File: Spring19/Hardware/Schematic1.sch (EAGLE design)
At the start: 18 parts

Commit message: Attempt 1 at routing
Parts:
- added R5: 1k, SparkFun-Resistors:1KOHM-0603-1/10W-1%
- added RELAYLEFT, RELAYRIGHT: (no value), con-lstb:MA07-1
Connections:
- new net N$14: IC1.2, R5.2, RELAYLEFT.1
- net GND: now also R5.1, RELAYLEFT.7
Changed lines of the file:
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@@
 <part name="GND3" library="supply1" library_urn="urn:adsk.eagle:library:371" deviceset="GND" device=""/>
 <part name="P+3" library="supply1" library_urn="urn:adsk.eagle:library:371" deviceset="VCC" device=""/>
+<part name="RELAYRIGHT" library="con-lstb" library_urn="urn:adsk.eagle:library:162" deviceset="MA07-1" device="" package3d_urn="urn:adsk.eagle:package:8341/1"/>
+<part name="RELAYLEFT" library="con-lstb" library_urn="urn:adsk.eagle:library:162" deviceset="MA07-1" device="" package3d_urn="urn:adsk.eagle:package:8341/1"/>
+<part name="GND9" library="supply1" library_urn="urn:adsk.eagle:library:371" deviceset="GND" device=""/>
+<part name="R5" library="SparkFun-Resistors" library_urn="urn:adsk.eagle:library:532" deviceset="1KOHM" device="-0603-1/10W-1%" package3d_urn="urn:adsk.eagle:package:39650/1" value="1k"/>
+<part name="GND10" library="supply1" library_urn="urn:adsk.eagle:library:371" deviceset="GND" device=""/>
 </parts>
 <sheets>
@@
 <instance part="P+3" gate="VCC" x="106.68" y="38.1" smashed="yes" rot="MR0">
 <attribute name="VALUE" x="109.22" y="35.56" size="1.778" layer="96" rot="MR90"/>
+</instance>
+<instance part="RELAYRIGHT" gate="1" x="187.96" y="-66.04" smashed="yes">
+<attribute name="VALUE" x="186.69" y="-78.74" size="1.778" layer="96"/>
+<attribute name="NAME" x="186.69" y="-55.118" size="1.778" layer="95"/>
+</instance>
+<instance part="RELAYLEFT" gate="1" x="182.88" y="-66.04" smashed="yes" rot="R180">
+<attribute name="VALUE" x="184.15" y="-53.34" size="1.778" layer="96" rot="R180"/>
+<attribute name="NAME" x="184.15" y="-76.962" size="1.778" layer="95" rot="R180"/>
+</instance>
+<instance part="GND9" gate="1" x="167.64" y="-73.66" smashed="yes" rot="MR90">
+<attribute name="VALUE" x="165.1" y="-76.2" size="1.778" layer="96" rot="MR90"/>
+</instance>
+<instance part="R5" gate="G$1" x="157.48" y="-58.42" smashed="yes" rot="MR90">
+<attribute name="NAME" x="159.004" y="-58.42" size="1.778" layer="95" font="vector" rot="MR90" align="bottom-center"/>
+<attribute name="VALUE" x="155.956" y="-58.42" size="1.778" layer="96" font="vector" rot="MR90" align="top-center"/>
+</instance>
+<instance part="GND10" gate="1" x="157.48" y="-68.58" smashed="yes" rot="MR0">
+<attribute name="VALUE" x="160.02" y="-71.12" size="1.778" layer="96" rot="MR0"/>
 </instance>
 </instances>
@@
 <pinref part="GND3" gate="1" pin="GND"/>
 <pinref part="IC1" gate="G$1" pin="GND@3"/>
+</segment>
+<segment>
+<pinref part="GND9" gate="1" pin="GND"/>
+<wire x1="175.26" y1="-73.66" x2="170.18" y2="-73.66" width="0.1524" layer="91"/>
+<pinref part="RELAYLEFT" gate="1" pin="7"/>
+</segment>
+<segment>
+<pinref part="GND10" gate="1" pin="GND"/>
+<wire x1="157.48" y1="-63.5" x2="157.48" y2="-66.04" width="0.1524" layer="91"/>
+<pinref part="R5" gate="G$1" pin="1"/>
 </segment>
 </net>
@@
 </segment>
 </net>
+<net name="N$14" class="0">
+<segment>
+<pinref part="RELAYLEFT" gate="1" pin="1"/>
+<wire x1="175.26" y1="-58.42" x2="175.26" y2="-53.34" width="0.1524" layer="91"/>
+<wire x1="175.26" y1="-53.34" x2="157.48" y2="-53.34" width="0.1524" layer="91"/>
+<wire x1="157.48" y1="-53.34" x2="134.62" y2="-53.34" width="0.1524" layer="91"/>
+<wire x1="134.62" y1="-53.34" x2="134.62" y2="17.78" width="0.1524" layer="91"/>
+<pinref part="IC1" gate="G$1" pin="2"/>
+<wire x1="134.62" y1="17.78" x2="129.54" y2="17.78" width="0.1524" layer="91"/>
+<pinref part="R5" gate="G$1" pin="2"/>
+<junction x="157.48" y="-53.34"/>
+</segment>
+</net>

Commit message: Finish routing
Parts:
- removed C1, C2: 22pF, SparkFun-Capacitors:22PF-0603-50V-5%
- removed CLOCK: 16MHz, SparkFun-Clocks:CRYSTAL-16MHZPTH-HC49US
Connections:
- removed net N$11: C2.2, CLOCK.1
- removed net N$13: C1.2, CLOCK.2
- net GND: no longer C1.1, C2.1
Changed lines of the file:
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@@
 <part name="SWITCH3" library="pinhead" library_urn="urn:adsk.eagle:library:325" deviceset="PINHD-1X2" device="" package3d_urn="urn:adsk.eagle:package:22435/2"/>
 <part name="CAP1188" library="pinhead" library_urn="urn:adsk.eagle:library:325" deviceset="PINHD-2X13" device="" package3d_urn="urn:adsk.eagle:package:22418/2"/>
-<part name="CLOCK" library="SparkFun-Clocks" library_urn="urn:adsk.eagle:library:511" deviceset="CRYSTAL-16MHZ" device="PTH-HC49US" package3d_urn="urn:adsk.eagle:package:37515/1" value="16MHz"/>
-<part name="C1" library="SparkFun-Capacitors" library_urn="urn:adsk.eagle:library:510" deviceset="22PF" device="-0603-50V-5%" package3d_urn="urn:adsk.eagle:package:37414/1" value="22pF"/>
-<part name="C2" library="SparkFun-Capacitors" library_urn="urn:adsk.eagle:library:510" deviceset="22PF" device="-0603-50V-5%" package3d_urn="urn:adsk.eagle:package:37414/1" value="22pF"/>
-<part name="GND6" library="supply1" library_urn="urn:adsk.eagle:library:371" deviceset="GND" device=""/>
 <part name="P+1" library="supply1" library_urn="urn:adsk.eagle:library:371" deviceset="VCC" device=""/>
 <part name="GND2" library="supply1" library_urn="urn:adsk.eagle:library:371" deviceset="GND" device=""/>
@@
 <attribute name="VALUE" x="196.85" y="-2.54" size="1.778" layer="96"/>
 </instance>
-<instance part="CLOCK" gate="G$1" x="139.7" y="-66.04" smashed="yes" rot="R90">
-<attribute name="NAME" x="137.668" y="-66.04" size="1.778" layer="95" font="vector" rot="R90" align="bottom-center"/>
-<attribute name="VALUE" x="141.732" y="-66.04" size="1.778" layer="96" font="vector" rot="R90" align="top-center"/>
-</instance>
-<instance part="C1" gate="G$1" x="132.08" y="-63.5" smashed="yes" rot="R90">
-<attribute name="NAME" x="129.159" y="-61.976" size="1.778" layer="95" font="vector" rot="R90"/>
-<attribute name="VALUE" x="134.239" y="-61.976" size="1.778" layer="96" font="vector" rot="R90"/>
-</instance>
-<instance part="C2" gate="G$1" x="132.08" y="-68.58" smashed="yes" rot="R90">
-<attribute name="NAME" x="129.159" y="-67.056" size="1.778" layer="95" font="vector" rot="R90"/>
-<attribute name="VALUE" x="134.239" y="-67.056" size="1.778" layer="96" font="vector" rot="R90"/>
-</instance>
-<instance part="GND6" gate="1" x="121.92" y="-68.58" smashed="yes">
-<attribute name="VALUE" x="119.38" y="-71.12" size="1.778" layer="96"/>
-</instance>
 <instance part="P+1" gate="VCC" x="218.44" y="-7.62" smashed="yes" rot="MR0">
 <attribute name="VALUE" x="220.98" y="-10.16" size="1.778" layer="96" rot="MR90"/>
@@
 </net>
 <net name="GND" class="0">
-<segment>
-<pinref part="C1" gate="G$1" pin="1"/>
-<pinref part="C2" gate="G$1" pin="1"/>
-<wire x1="127" y1="-63.5" x2="127" y2="-66.04" width="0.1524" layer="91"/>
-<wire x1="127" y1="-66.04" x2="127" y2="-68.58" width="0.1524" layer="91"/>
-<wire x1="127" y1="-66.04" x2="121.92" y2="-66.04" width="0.1524" layer="91"/>
-<junction x="127" y="-66.04"/>
-<pinref part="GND6" gate="1" pin="GND"/>
-</segment>
 <segment>
 <pinref part="R1" gate="G$1" pin="2"/>
@@
 </segment>
 </net>
-<net name="N$11" class="0">
-<segment>
-<wire x1="134.62" y1="-68.58" x2="139.7" y2="-68.58" width="0.1524" layer="91"/>
-<pinref part="CLOCK" gate="G$1" pin="1"/>
-<pinref part="C2" gate="G$1" pin="2"/>
-</segment>
-</net>
-<net name="N$13" class="0">
-<segment>
-<pinref part="CLOCK" gate="G$1" pin="2"/>
-<pinref part="C1" gate="G$1" pin="2"/>
-<wire x1="139.7" y1="-63.5" x2="134.62" y2="-63.5" width="0.1524" layer="91"/>
-</segment>
-</net>

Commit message: Add through holes for plug
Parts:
- added X1: SSW-101-02-G-D, con-samtec:SSW-101-02-G-D
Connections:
- new net N$11: RELAYRIGHT.6, X1-1.1
- new net N$13: RELAYRIGHT.2, X1-2.1
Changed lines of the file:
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@@
 <part name="R5" library="SparkFun-Resistors" library_urn="urn:adsk.eagle:library:532" deviceset="1KOHM" device="-0603-1/10W-1%" package3d_urn="urn:adsk.eagle:package:39650/1" value="1k"/>
 <part name="GND10" library="supply1" library_urn="urn:adsk.eagle:library:371" deviceset="GND" device=""/>
+<part name="X1" library="con-samtec" library_urn="urn:adsk.eagle:library:184" deviceset="SSW-101-02-G" device="-D"/>
 </parts>
 <sheets>
@@
 <instance part="GND10" gate="1" x="157.48" y="-68.58" smashed="yes" rot="MR0">
 <attribute name="VALUE" x="160.02" y="-71.12" size="1.778" layer="96" rot="MR0"/>
+</instance>
+<instance part="X1" gate="-1" x="215.9" y="-58.42" smashed="yes">
+<attribute name="VALUE" x="213.36" y="-55.88" size="1.778" layer="96"/>
+<attribute name="NAME" x="212.852" y="-57.658" size="1.524" layer="95" rot="R180"/>
+</instance>
+<instance part="X1" gate="-2" x="236.22" y="-58.42" smashed="yes">
+<attribute name="NAME" x="233.172" y="-57.658" size="1.524" layer="95" rot="R180"/>
 </instance>
 </instances>
@@
 </segment>
 </net>
+<net name="N$11" class="0">
+<segment>
+<pinref part="RELAYRIGHT" gate="1" pin="6"/>
+<wire x1="195.58" y1="-60.96" x2="218.44" y2="-60.96" width="0.1524" layer="91"/>
+<pinref part="X1" gate="-1" pin="1"/>
+<wire x1="218.44" y1="-60.96" x2="218.44" y2="-58.42" width="0.1524" layer="91"/>
+</segment>
+</net>
+<net name="N$13" class="0">
+<segment>
+<pinref part="X1" gate="-2" pin="1"/>
+<wire x1="238.76" y1="-58.42" x2="238.76" y2="-71.12" width="0.1524" layer="91"/>
+<pinref part="RELAYRIGHT" gate="1" pin="2"/>
+<wire x1="238.76" y1="-71.12" x2="195.58" y2="-71.12" width="0.1524" layer="91"/>
+</segment>
+</net>

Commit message: Adjust cap1188 footprint and add some bottom routes
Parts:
- removed CAP1188: (no value), pinhead:PINHD-2X13
- added CAPLEFT, CAPRIGHT: (no value), con-lstb:MA13-1
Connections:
- net GND: now also CAPLEFT.10; no longer CAP1188.7
- net N$7: now also CAPLEFT.13; no longer CAP1188.1
- net N$8: now also CAPLEFT.12; no longer CAP1188.3
- net VCC: now also CAPLEFT.11; no longer CAP1188.5
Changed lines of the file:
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@@
 <part name="SWITCH2" library="pinhead" library_urn="urn:adsk.eagle:library:325" deviceset="PINHD-1X2" device="" package3d_urn="urn:adsk.eagle:package:22435/2"/>
 <part name="SWITCH3" library="pinhead" library_urn="urn:adsk.eagle:library:325" deviceset="PINHD-1X2" device="" package3d_urn="urn:adsk.eagle:package:22435/2"/>
-<part name="CAP1188" library="pinhead" library_urn="urn:adsk.eagle:library:325" deviceset="PINHD-2X13" device="" package3d_urn="urn:adsk.eagle:package:22418/2"/>
 <part name="P+1" library="supply1" library_urn="urn:adsk.eagle:library:371" deviceset="VCC" device=""/>
 <part name="GND2" library="supply1" library_urn="urn:adsk.eagle:library:371" deviceset="GND" device=""/>
@@
 <part name="GND10" library="supply1" library_urn="urn:adsk.eagle:library:371" deviceset="GND" device=""/>
 <part name="X1" library="con-samtec" library_urn="urn:adsk.eagle:library:184" deviceset="SSW-101-02-G" device="-D"/>
-<part name="U$1" library="relay" deviceset="RELAY" device=""/>
+<part name="CAPRIGHT" library="con-lstb" library_urn="urn:adsk.eagle:library:162" deviceset="MA13-1" device="" package3d_urn="urn:adsk.eagle:package:8367/1"/>
+<part name="CAPLEFT" library="con-lstb" library_urn="urn:adsk.eagle:library:162" deviceset="MA13-1" device="" package3d_urn="urn:adsk.eagle:package:8367/1"/>
 </parts>
 <sheets>
@@
 <attribute name="VALUE" x="194.31" y="-48.26" size="1.778" layer="96"/>
 </instance>
-<instance part="CAP1188" gate="A" x="203.2" y="17.78" smashed="yes">
-<attribute name="NAME" x="196.85" y="36.195" size="1.778" layer="95"/>
-<attribute name="VALUE" x="196.85" y="-2.54" size="1.778" layer="96"/>
-</instance>
 <instance part="P+1" gate="VCC" x="218.44" y="-7.62" smashed="yes" rot="MR0">
 <attribute name="VALUE" x="220.98" y="-10.16" size="1.778" layer="96" rot="MR90"/>
@@
 </instance>
 <instance part="GND7" gate="1" x="193.04" y="-5.08" smashed="yes" rot="MR270">
-<attribute name="VALUE" x="195.58" y="-2.54" size="1.778" layer="96" rot="MR270"/>
+<attribute name="VALUE" x="215.9" y="35.56" size="1.778" layer="96" rot="MR270"/>
 </instance>
 <instance part="POTENTIOMETER" gate="G$1" x="175.26" y="38.1" smashed="yes" rot="R180">
@@
 <instance part="X1" gate="-2" x="236.22" y="-58.42" smashed="yes">
 <attribute name="NAME" x="233.172" y="-57.658" size="1.524" layer="95" rot="R180"/>
+</instance>
+<instance part="CAPRIGHT" gate="G$1" x="238.76" y="17.78" smashed="yes">
+<attribute name="VALUE" x="237.49" y="-2.54" size="1.778" layer="96"/>
+<attribute name="NAME" x="237.49" y="36.322" size="1.778" layer="95"/>
+</instance>
+<instance part="CAPLEFT" gate="G$1" x="223.52" y="17.78" smashed="yes" rot="MR0">
+<attribute name="VALUE" x="224.79" y="-2.54" size="1.778" layer="96" rot="MR0"/>
+<attribute name="NAME" x="224.79" y="36.322" size="1.778" layer="95" rot="MR0"/>
 </instance>
 </instances>
@@
 </segment>
 <segment>
-<pinref part="CAP1188" gate="A" pin="7"/>
-<wire x1="200.66" y1="25.4" x2="190.5" y2="25.4" width="0.1524" layer="91"/>
+<wire x1="215.9" y1="25.4" x2="190.5" y2="25.4" width="0.1524" layer="91"/>
 <pinref part="GND2" gate="1" pin="GND"/>
+<pinref part="CAPLEFT" gate="G$1" pin="10"/>
 </segment>
 <segment>
@@
 </segment>
 <segment>
-<pinref part="CAP1188" gate="A" pin="5"/>
-<wire x1="200.66" y1="27.94" x2="195.58" y2="27.94" width="0.1524" layer="91"/>
-<pinref part="P+2" gate="VCC" pin="VCC"/>
-</segment>
-<segment>
 <wire x1="165.1" y1="10.16" x2="157.48" y2="10.16" width="0.1524" layer="91"/>
 <pinref part="P+4" gate="VCC" pin="VCC"/>
@@
 <pinref part="IC1" gate="G$1" pin="+5V"/>
 </segment>
+<segment>
+<pinref part="P+2" gate="VCC" pin="VCC"/>
+<pinref part="CAPLEFT" gate="G$1" pin="11"/>
+<wire x1="195.58" y1="27.94" x2="215.9" y2="27.94" width="0.1524" layer="91"/>
+</segment>
 </net>
 <net name="N$7" class="0">
@@
 <wire x1="152.4" y1="25.4" x2="180.34" y2="25.4" width="0.1524" layer="91"/>
 <wire x1="180.34" y1="25.4" x2="180.34" y2="33.02" width="0.1524" layer="91"/>
-<pinref part="CAP1188" gate="A" pin="1"/>
-<wire x1="180.34" y1="33.02" x2="200.66" y2="33.02" width="0.1524" layer="91"/>
+<wire x1="180.34" y1="33.02" x2="190.5" y2="33.02" width="0.1524" layer="91"/>
 <pinref part="IC1" gate="G$1" pin="A4"/>
 <wire x1="93.98" y1="0" x2="78.74" y2="0" width="0.1524" layer="91"/>
@@
 <wire x1="78.74" y1="38.1" x2="152.4" y2="38.1" width="0.1524" layer="91"/>
 <wire x1="152.4" y1="38.1" x2="152.4" y2="25.4" width="0.1524" layer="91"/>
+<wire x1="190.5" y1="33.02" x2="190.5" y2="40.64" width="0.1524" layer="91"/>
+<wire x1="190.5" y1="40.64" x2="215.9" y2="40.64" width="0.1524" layer="91"/>
+<pinref part="CAPLEFT" gate="G$1" pin="13"/>
+<wire x1="215.9" y1="40.64" x2="215.9" y2="33.02" width="0.1524" layer="91"/>
 </segment>
 </net>
@@
 <wire x1="149.86" y1="22.86" x2="182.88" y2="22.86" width="0.1524" layer="91"/>
 <wire x1="182.88" y1="22.86" x2="182.88" y2="30.48" width="0.1524" layer="91"/>
-<pinref part="CAP1188" gate="A" pin="3"/>
-<wire x1="182.88" y1="30.48" x2="200.66" y2="30.48" width="0.1524" layer="91"/>
+<wire x1="182.88" y1="30.48" x2="193.04" y2="30.48" width="0.1524" layer="91"/>
 <pinref part="IC1" gate="G$1" pin="A5"/>
 <wire x1="93.98" y1="-2.54" x2="73.66" y2="-2.54" width="0.1524" layer="91"/>
@@
 <wire x1="73.66" y1="33.02" x2="149.86" y2="33.02" width="0.1524" layer="91"/>
 <wire x1="149.86" y1="33.02" x2="149.86" y2="22.86" width="0.1524" layer="91"/>
-</segment>
-</net>
+<wire x1="193.04" y1="30.48" x2="193.04" y2="38.1" width="0.1524" layer="91"/>
+<wire x1="193.04" y1="38.1" x2="213.36" y2="38.1" width="0.1524" layer="91"/>
+<pinref part="CAPLEFT" gate="G$1" pin="12"/>
+<wire x1="213.36" y1="38.1" x2="213.36" y2="30.48" width="0.1524" layer="91"/>
+<wire x1="213.36" y1="30.48" x2="215.9" y2="30.48" width="0.1524" layer="91"/>
+</segment>
+</net>

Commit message: PCB for etching
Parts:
- removed CAPLEFT, CAPRIGHT: (no value), con-lstb:MA13-1
- removed SWITCH1, SWITCH2, SWITCH3: (no value), pinhead:PINHD-1X2
- added SV1, SV2, SV3: (no value), con-lstb:MA03-1
- added SV4: (no value), con-lstb:MA04-1
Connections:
- net GND: now also SV4.4; no longer CAPLEFT.10
- net N$10: now also SV3.1; no longer SWITCH3.1
- net N$4: now also SV1.1; no longer SWITCH2.1
- net N$5: now also SV2.1; no longer SWITCH1.1
- net N$7: now also SV4.1; no longer CAPLEFT.13
- net N$8: now also SV4.2; no longer CAPLEFT.12
- net VCC: now also SV1.2, SV2.2, SV3.2, SV4.3; no longer CAPLEFT.11, SWITCH1.2, SWITCH2.2, SWITCH3.2

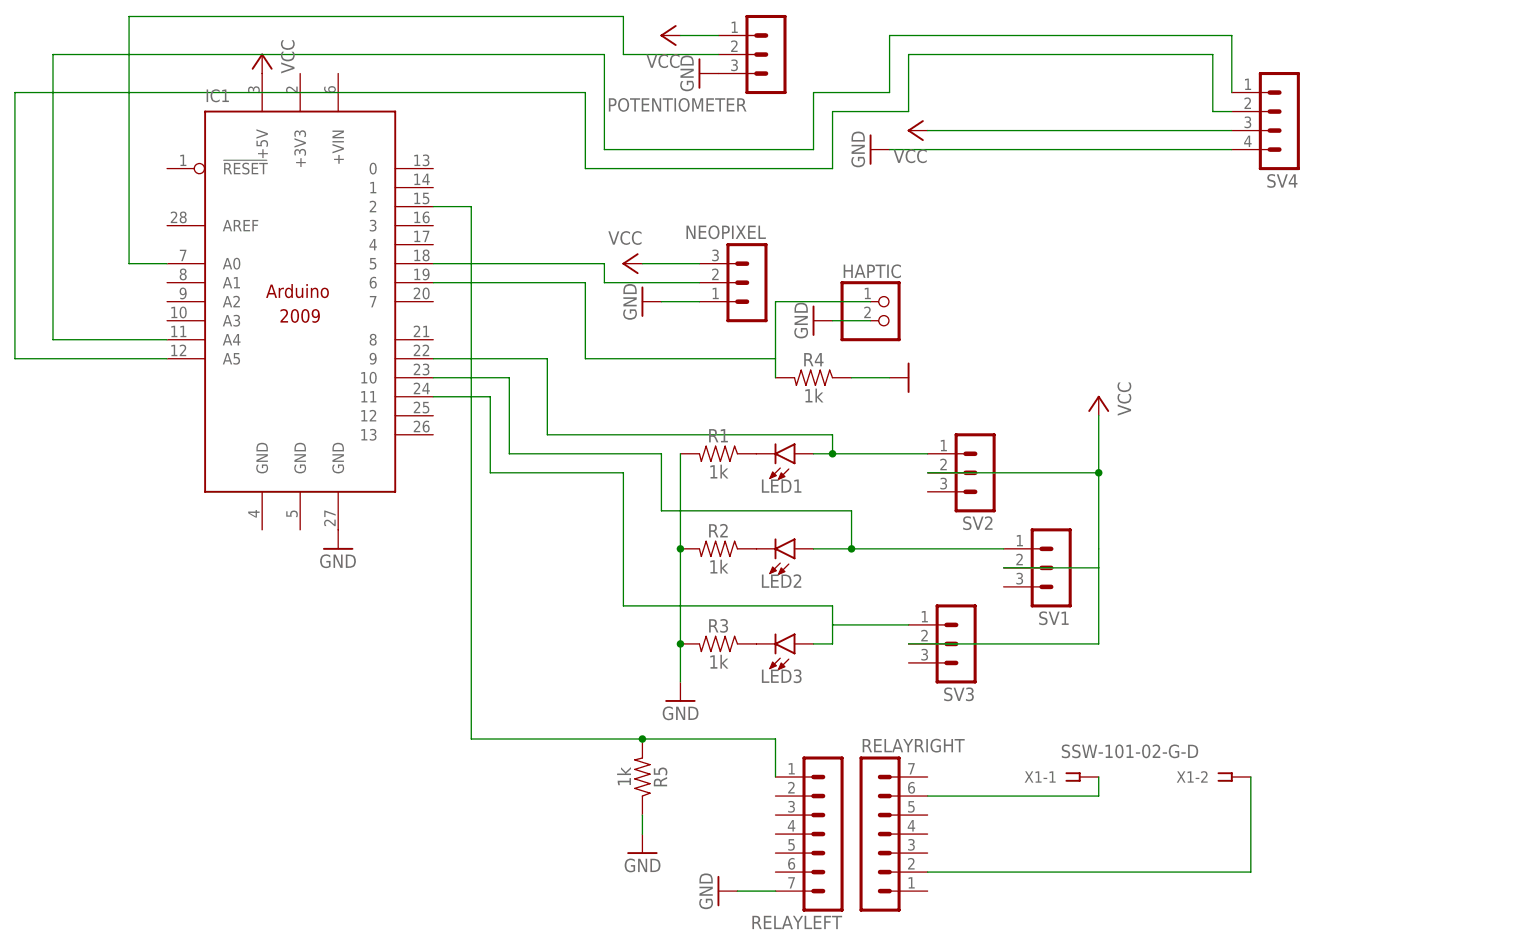
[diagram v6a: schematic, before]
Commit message: Switch relay direction
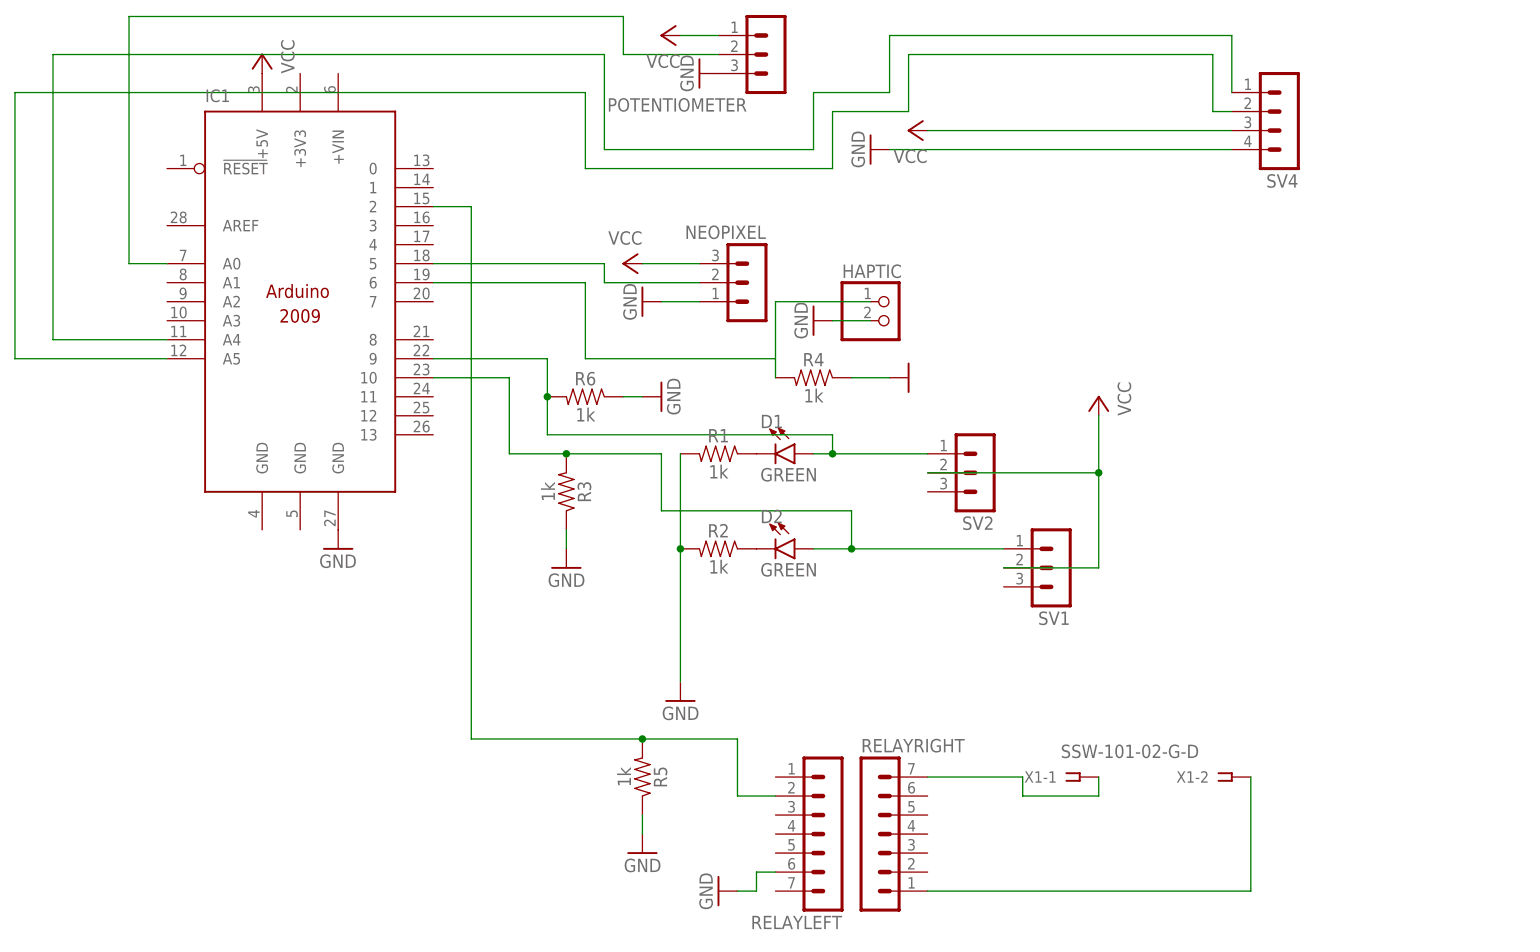
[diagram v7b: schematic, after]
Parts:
- removed LED1, LED2, LED3: (no value), SparkFun-LED:LED3MM
- removed SV3: (no value), con-lstb:MA03-1
- added D1, D2: GREEN, SparkFun-LED:LED-GREEN1206
- added R6: 1k, SparkFun-Resistors:1KOHM-0603-1/10W-1%
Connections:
- removed net N$10: IC1.11, LED3.A, SV3.1
- removed net N$3: LED3.C, R3.1
- net GND: now also R3.1, R6.1, RELAYLEFT.6; no longer R3.2, RELAYLEFT.7
- net N$1: now also D1.C; no longer LED1.C
- net N$11: now also RELAYRIGHT.7; no longer RELAYRIGHT.6
- net N$13: now also RELAYRIGHT.1; no longer RELAYRIGHT.2
- net N$14: now also RELAYLEFT.2; no longer RELAYLEFT.1
- net N$2: now also D2.C; no longer LED2.C
- net N$4: now also D2.A, R3.2; no longer LED2.A
- net N$5: now also D1.A, R6.2; no longer LED1.A
- net VCC: no longer SV3.2
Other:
- moved on the sheet: R3
